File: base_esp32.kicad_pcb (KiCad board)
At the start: 2 copper layers, 100 x 100 mm, 73 parts, among them J1 Input Source, J10 H_IO15_OUT, J11 H_IO32_OUT, J12 H_IO02_OUT, J13 H_IO04_OUT, J14 5V, J15 5V, J16 H_3V3_1, J17 H_IO34, J18 H_IO35, J19 H_IO36, J2 BYPASS_SRC_5V, J20 H_IO39, J21 S_3V3_1, J22 H_3V3_2, J23 H_KEYPAD, J24 H_I2C, J25 H_SPI, J26 TX_RX, J27 S_3V3_2, J28 H_GND, J29 S_KEYPAD, J3 BYPASS_SRC_3V3, J30 S_I2C, J31 S_SPI, J32 S_GND, J33 Src Board, J4 H_IO33, J5 H_IO15, J6 H_IO32, J7 H_IO02, J8 H_IO04, J9 H_IO33_OUT, SW1 INPUT_D1, SW2 INPUT_D2, SW3 SW_DIP_INPUTS, SW4 ENABLE, SW5 SW_DIP_KEYPAD, SW6 Selector_Input, SW7 Selector_Input, SW8 BOOT, U1 LM7805_TO220, U2 AMS1117, U3 AMS1117, U4 ESP32-DevKitC

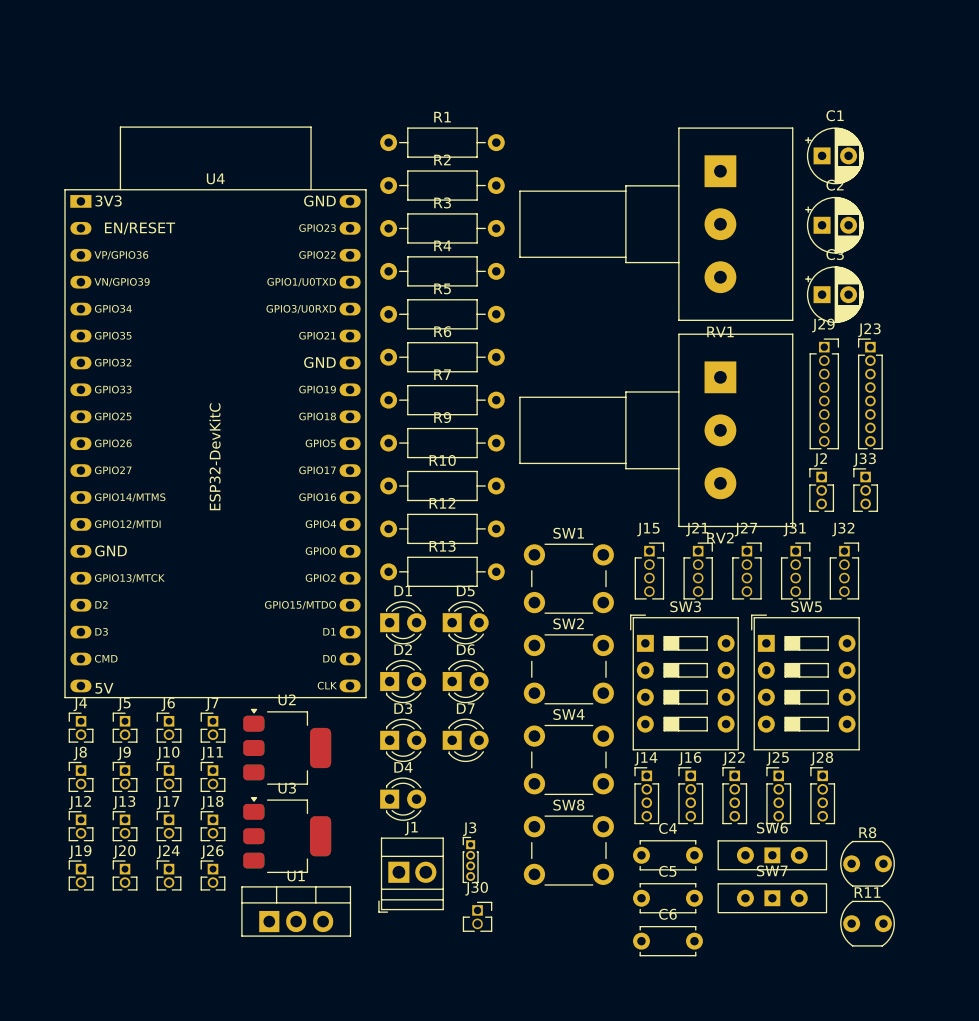
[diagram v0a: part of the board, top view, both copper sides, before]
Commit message: fix: package to sw5 dip
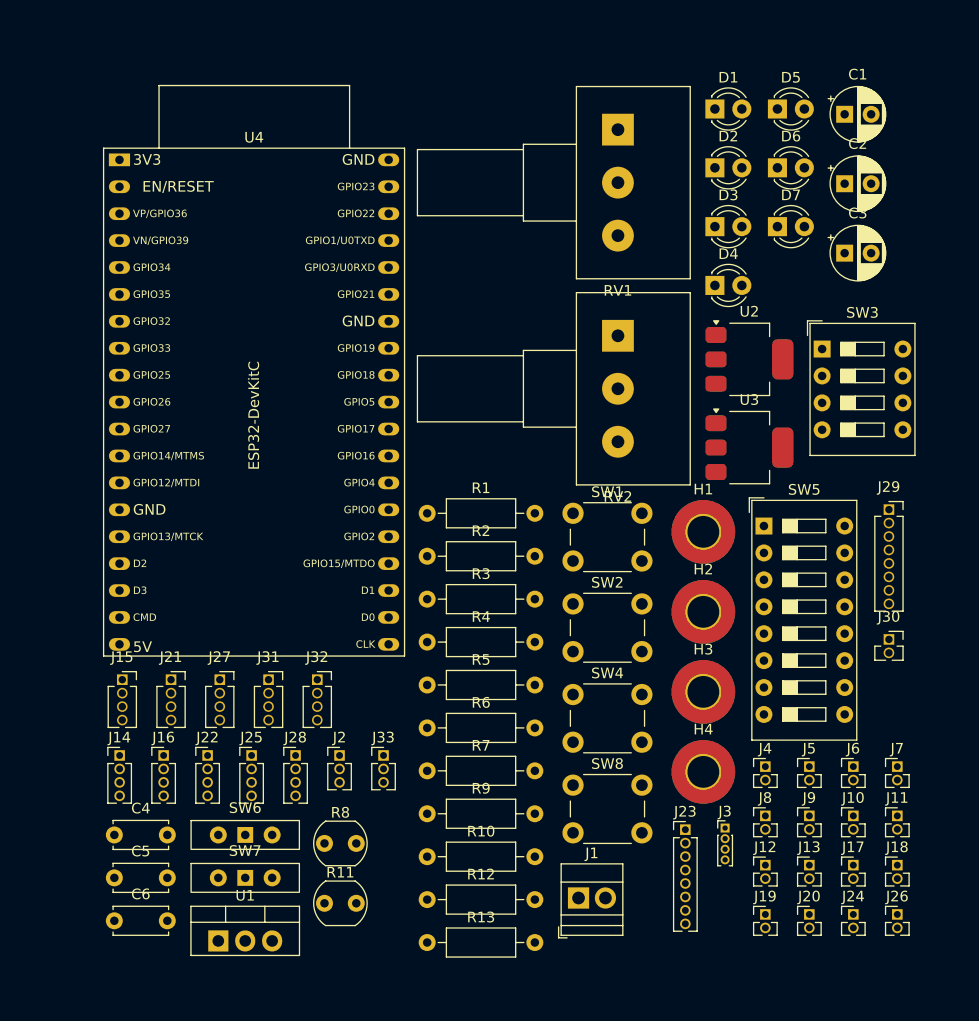
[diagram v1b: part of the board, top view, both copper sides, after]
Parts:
- added H1: MountingHole_Pad, MountingHole:MountingHole_3mm_Pad_TopBottom, F.Cu at (170.3, 101.3)
- added H2: MountingHole_Pad, MountingHole:MountingHole_3mm_Pad_TopBottom, F.Cu at (170.3, 108.9)
- added H3: MountingHole_Pad, MountingHole:MountingHole_3mm_Pad_TopBottom, F.Cu at (170.3, 116.4)
- added H4: MountingHole_Pad, MountingHole:MountingHole_3mm_Pad_TopBottom, F.Cu at (170.3, 124.0)
- SW5: footprint Button_Switch_THT:SW_DIP_SPSTx04_Slide_9.78x12.34mm_W7.62mm_P2.54mm -> Button_Switch_THT:SW_DIP_SPSTx08_Slide_9.78x22.5mm_W7.62mm_P2.54mm
- moved J10 64.7 mm to (184.5, 128.1)
- moved J11 64.7 mm to (188.6, 128.1)
- moved J13 64.7 mm to (180.3, 132.8)
- moved J17 64.7 mm to (184.5, 132.8)
- moved J18 64.7 mm to (188.6, 132.8)
- moved J20 64.7 mm to (180.3, 137.4)
- moved J24 64.7 mm to (184.5, 137.4)
- moved J26 64.7 mm to (188.6, 137.4)
- moved J5 64.7 mm to (180.3, 123.5)
- moved J6 64.7 mm to (184.5, 123.5)
- moved J7 64.7 mm to (188.6, 123.5)
- moved J9 64.7 mm to (180.3, 128.1)
- moved J12 64.7 mm to (176.2, 132.8)
- moved J19 64.7 mm to (176.2, 137.4)
- moved J4 64.7 mm to (176.2, 123.5)
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
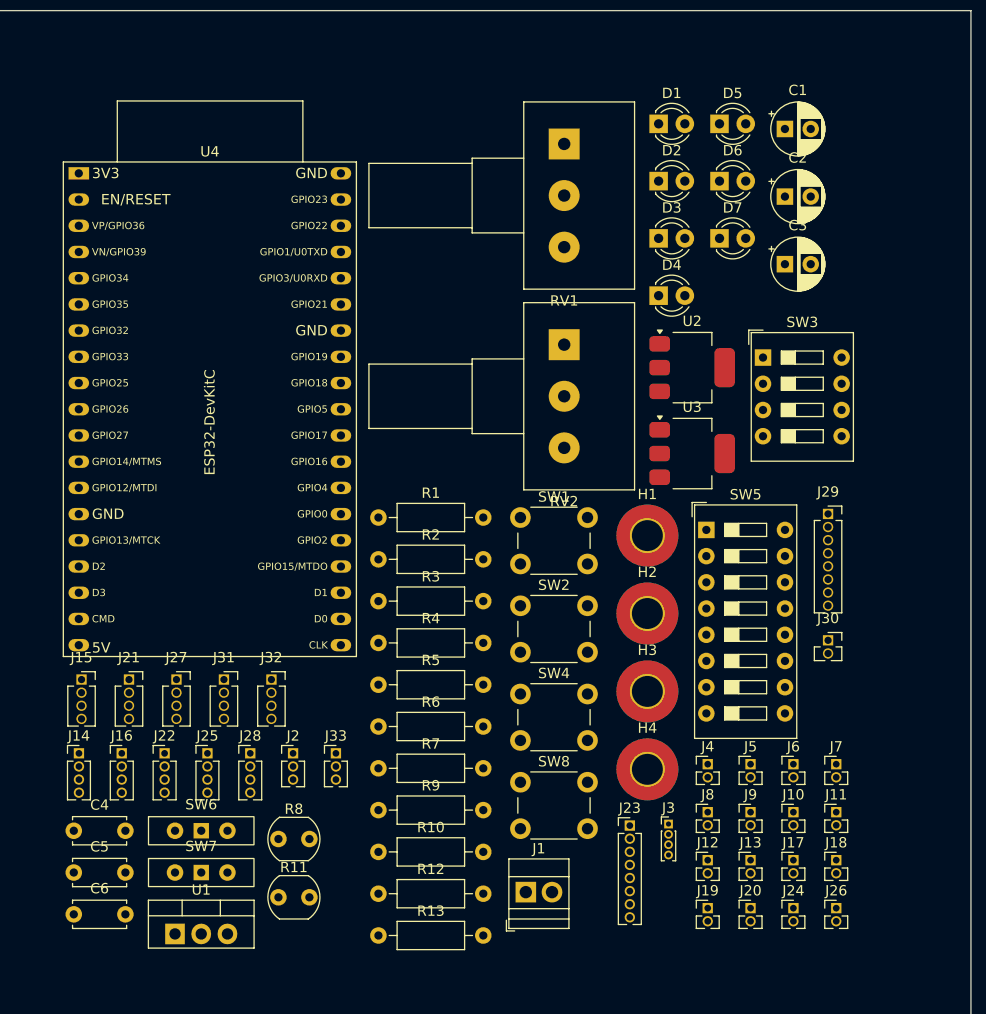
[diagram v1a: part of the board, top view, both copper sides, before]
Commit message: fix: footprints
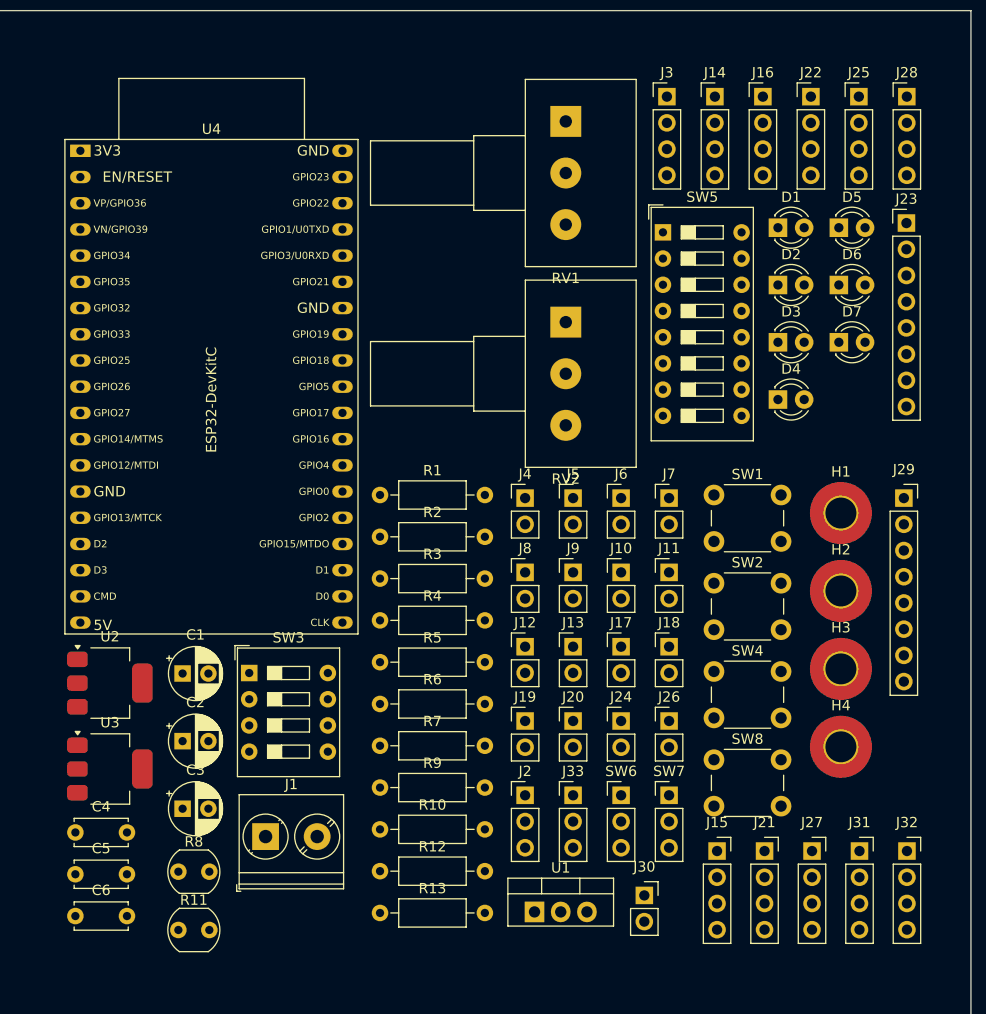
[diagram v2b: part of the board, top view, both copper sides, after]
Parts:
- J1: footprint TerminalBlock:TerminalBlock_Xinya_XY308-2.54-2P_1x02_P2.54mm_Horizontal -> TerminalBlock_Phoenix:TerminalBlock_Phoenix_PT-1,5-2-5.0-H_1x02_P5.00mm_Horizontal
- J10, J11, J12, J13, J17, J18, J19, J20, J24, J26, J4, J5, J6, J7, J8, J9: footprint Connector_PinHeader_1.27mm:PinHeader_1x02_P1.27mm_Vertical -> Connector_PinHeader_2.54mm:PinHeader_1x02_P2.54mm_Vertical
- J14: value 5V -> H_5V; footprint Connector_PinHeader_1.27mm:PinHeader_1x04_P1.27mm_Vertical -> Connector_PinHeader_2.54mm:PinHeader_1x04_P2.54mm_Vertical
- J15: value 5V -> S_5V; footprint Connector_PinSocket_1.27mm:PinSocket_1x04_P1.27mm_Vertical -> Connector_PinSocket_2.54mm:PinSocket_1x04_P2.54mm_Vertical
- J16, J22, J25, J28: footprint Connector_PinHeader_1.27mm:PinHeader_1x04_P1.27mm_Vertical -> Connector_PinHeader_2.54mm:PinHeader_1x04_P2.54mm_Vertical
- J2: footprint Connector_PinHeader_1.27mm:PinHeader_1x03_P1.27mm_Vertical -> Connector_PinHeader_2.54mm:PinHeader_1x03_P2.54mm_Vertical
- J21, J27, J31, J32: footprint Connector_PinSocket_1.27mm:PinSocket_1x04_P1.27mm_Vertical -> Connector_PinSocket_2.54mm:PinSocket_1x04_P2.54mm_Vertical
- J23: footprint Connector_PinHeader_1.27mm:PinHeader_1x08_P1.27mm_Vertical -> Connector_PinHeader_2.54mm:PinHeader_1x08_P2.54mm_Vertical
- J29: footprint Connector_PinSocket_1.27mm:PinSocket_1x08_P1.27mm_Vertical -> Connector_PinSocket_2.54mm:PinSocket_1x08_P2.54mm_Vertical
- J3: footprint Connector_PinHeader_1.00mm:PinHeader_1x04_P1.00mm_Vertical -> Connector_PinHeader_2.54mm:PinHeader_1x04_P2.54mm_Vertical
- J30: footprint Connector_PinSocket_1.27mm:PinSocket_1x02_P1.27mm_Vertical -> Connector_PinSocket_2.54mm:PinSocket_1x02_P2.54mm_Vertical
- J33: value Src Board -> H_Src Board; footprint Connector_PinHeader_1.27mm:PinHeader_1x03_P1.27mm_Vertical -> Connector_PinHeader_2.54mm:PinHeader_1x03_P2.54mm_Vertical
- SW6, SW7: footprint Button_Switch_THT:SW_Slide-03_Wuerth-WS-SLTV_10x2.5x6.4_P2.54mm -> Connector_PinHeader_2.54mm:PinHeader_1x03_P2.54mm_Vertical
- moved J28 90.0 mm to (195.5, 58.8)
- moved J25 89.6 mm to (190.8, 58.8)
- moved J22 89.3 mm to (186.2, 58.8)
- moved J16 88.9 mm to (181.5, 58.8)
- moved J14 88.6 mm to (176.9, 58.8)
- moved C1 78.7 mm to (125.3, 114.7)
- moved C2 78.7 mm to (125.3, 121.2)
- moved C3 78.7 mm to (125.3, 127.8)
- moved J3 70.5 mm to (172.2, 58.8)
- moved J23 64.2 mm to (195.4, 71.0)
- moved U2 64.2 mm to (118.3, 115.6)
- moved U3 64.2 mm to (118.3, 123.9)
- moved J27 63.8 mm to (186.3, 131.9)
- moved J31 63.8 mm to (190.9, 131.9)
- moved J32 63.8 mm to (195.5, 131.9)
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
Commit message: fix: some tags for pcb, sorting elements
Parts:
- D6: value LED -> LED EXT
- D7: value LED -> LED BOARD
- J2: value BYPASS_SRC_5V -> BYPASS SRC 5V
- J3: value BYPASS_SRC_3V3 -> BYPASS SRC 3V3
- RV2: value POT_1 -> POT_2; footprint Potentiometer_THT:Potentiometer_Alps_RK163_Single_Horizontal -> Potentiometer_THT:Potentiometer_Piher_PT-10-V05_Vertical
- SW6: value Selector_Input -> Selector Input 1
- SW7: value Selector_Input -> Selector Input 2
- moved J15 163.3 mm to (17.8, 96.0)
- moved J21 161.0 mm to (24.8, 96.0)
- moved J27 158.7 mm to (31.8, 96.0)
- moved J31 156.3 mm to (38.7, 96.0)
- moved J32 154.0 mm to (45.7, 96.0)
- moved J2 138.3 mm to (20.4, 119.5)
- moved J12 123.6 mm to (40.6, 74.9)
- moved J13 121.0 mm to (48.0, 74.9)
- moved J14 119.7 mm to (64.8, 100.6)
- moved J17 118.5 mm to (55.3, 74.9)
- moved J16 116.5 mm to (72.8, 100.6)
- moved J18 115.9 mm to (62.6, 74.9)
- moved J33 113.8 mm to (49.5, 119.4)
- moved J22 113.3 mm to (80.9, 100.6)
- moved J3 110.7 mm to (63.5, 38.1)
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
